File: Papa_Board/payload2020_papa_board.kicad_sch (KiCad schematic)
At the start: 14 parts, among them J12 Conn_01x05, J2 Conn_01x05, J3 Conn_01x05_Female, J4 Conn_01x05, J5 M80-5000642, J6 M80-5000642

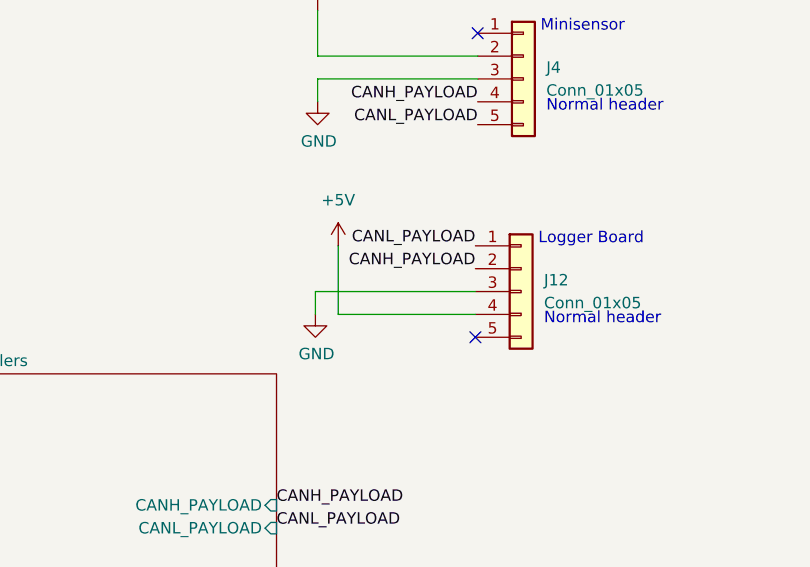
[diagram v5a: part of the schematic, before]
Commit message: moved LEDs made a bunch of nitpicky silkscreen & trace routing changes in an attempt to make things neater
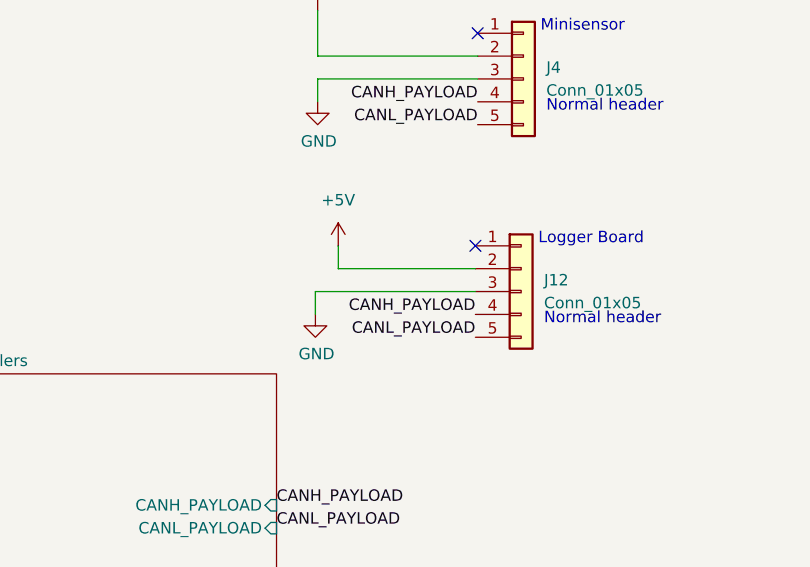
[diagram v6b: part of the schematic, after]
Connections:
- net +5V: now also J12.2 (Pin_2); no longer J12.4 (Pin_4)
- net CANH_PAYLOAD: now also J12.4 (Pin_4); no longer J12.2 (Pin_2)
- net CANL_PAYLOAD: now also J12.5 (Pin_5); no longer J12.1 (Pin_1)
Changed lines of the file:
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@@
   )
   (no_connect (at 261.874 89.154))
-  (no_connect (at 167.64 66.04))
   (no_connect (at 44.704 118.364))
   (no_connect (at 261.874 119.634))
   (no_connect (at 167.894 32.258))
+  (no_connect (at 167.64 55.88))
   (no_connect (at 44.704 120.904))
   (wire (pts (xy 35.56 76.2) (xy 43.18 76.2))
@@
     (stroke (width 0) (type default) (color 0 0 0 0))
   )
-  (wire (pts (xy 152.4 63.5) (xy 167.64 63.5))
+  (wire (pts (xy 152.4 58.42) (xy 167.64 58.42))
     (stroke (width 0) (type default) (color 0 0 0 0))
   )
@@
     (stroke (width 0) (type default) (color 0 0 0 0))
   )
-  (wire (pts (xy 152.4 55.88) (xy 152.4 63.5))
+  (wire (pts (xy 152.4 55.88) (xy 152.4 58.42))
     (stroke (width 0) (type default) (color 0 0 0 0))
   )
@@
     (effects (font (size 1.27 1.27)) (justify right bottom))
   )
-  (label "CANH_PAYLOAD" (at 167.64 58.42 180)
+  (label "CANH_PAYLOAD" (at 167.64 63.5 180)
     (effects (font (size 1.27 1.27)) (justify right bottom))
   )
@@
     (effects (font (size 1.27 1.27)) (justify right bottom))
   )
-  (label "CANL_PAYLOAD" (at 167.64 55.88 180)
-    (effects (font (size 1.27 1.27)) (justify right bottom))
-  )
+  (label "CANL_PAYLOAD" (at 167.64 66.04 180)
+    (effects (font (size 1.27 1.27)) (justify right bottom))
+  )

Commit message: addressed joe's concerns
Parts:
- J2: value Conn_01x05 -> Conn_02x06
- J3: value Conn_01x05_Female -> Conn_02x06
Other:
- sheet Logger board renamed SD Card
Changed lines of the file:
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@@
     (in_bom yes) (on_board yes)
     (property "Reference" "J2" (id 0) (at 35.814 110.744 0))
-    (property "Value" "Conn_01x05" (id 1) (at 35.814 113.284 0))
+    (property "Value" "Conn_02x06" (id 1) (at 35.814 113.284 0))
     (property "Footprint" "Payload2020_custom:connector_Harwin_M80-5000642" (id 2) (at 39.624 123.444 0)
       (effects (font (size 1.27 1.27)) hide)
@@
     (in_bom yes) (on_board yes)
     (property "Reference" "J3" (id 0) (at 33.02 68.58 0))
-    (property "Value" "Conn_01x05_Female" (id 1) (at 33.02 71.12 0))
+    (property "Value" "Conn_02x06" (id 1) (at 33.02 71.12 0))
     (property "Footprint" "Connector_PinHeader_2.54mm:PinHeader_1x05_P2.54mm_Vertical" (id 2) (at 30.48 81.28 0)
       (effects (font (size 1.27 1.27)) hide)
@@
     (stroke (width 0) (type solid) (color 0 0 0 0))
     (fill (color 0 0 0 0.0000))
-    (property "Sheet name" "Logger board" (id 0) (at 155.702 132.8924 0)
+    (property "Sheet name" "SD Card" (id 0) (at 155.702 132.8924 0)
       (effects (font (size 1.27 1.27)) (justify left bottom))
     )
@@
     )
     (path "/00000000-0000-0000-0000-00005ff6c4e6"
-      (reference "J2") (unit 1) (value "Conn_01x05") (footprint "Payload2020_custom:connector_Harwin_M80-5000642")
+      (reference "J2") (unit 1) (value "Conn_02x06") (footprint "Payload2020_custom:connector_Harwin_M80-5000642")
     )
     (path "/00000000-0000-0000-0000-000060a00e19"
-      (reference "J3") (unit 1) (value "Conn_01x05_Female") (footprint "Connector_PinHeader_2.54mm:PinHeader_1x05_P2.54mm_Vertical")
+      (reference "J3") (unit 1) (value "Conn_02x06") (footprint "Connector_PinHeader_2.54mm:PinHeader_1x05_P2.54mm_Vertical")
     )
     (path "/00000000-0000-0000-0000-00006000b832"
